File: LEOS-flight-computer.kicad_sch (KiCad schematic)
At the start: 7 parts, among them J3 GPIO

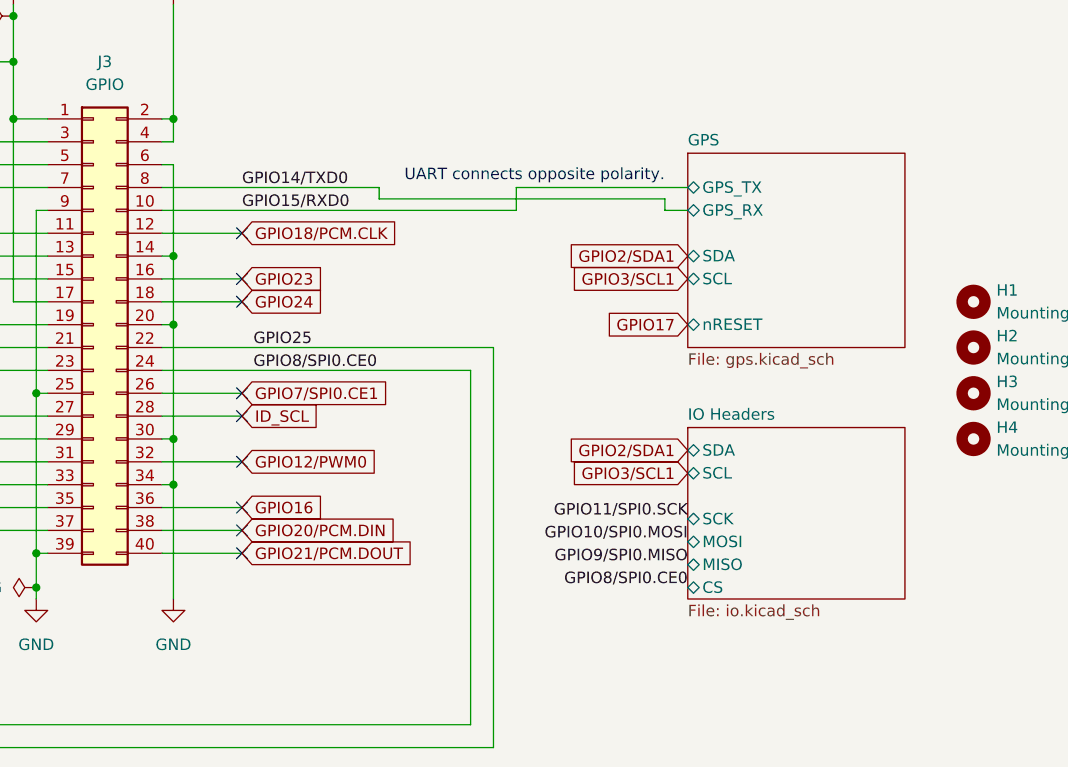
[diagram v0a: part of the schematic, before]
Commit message: v2.2 with added indicator LEDs and a user button
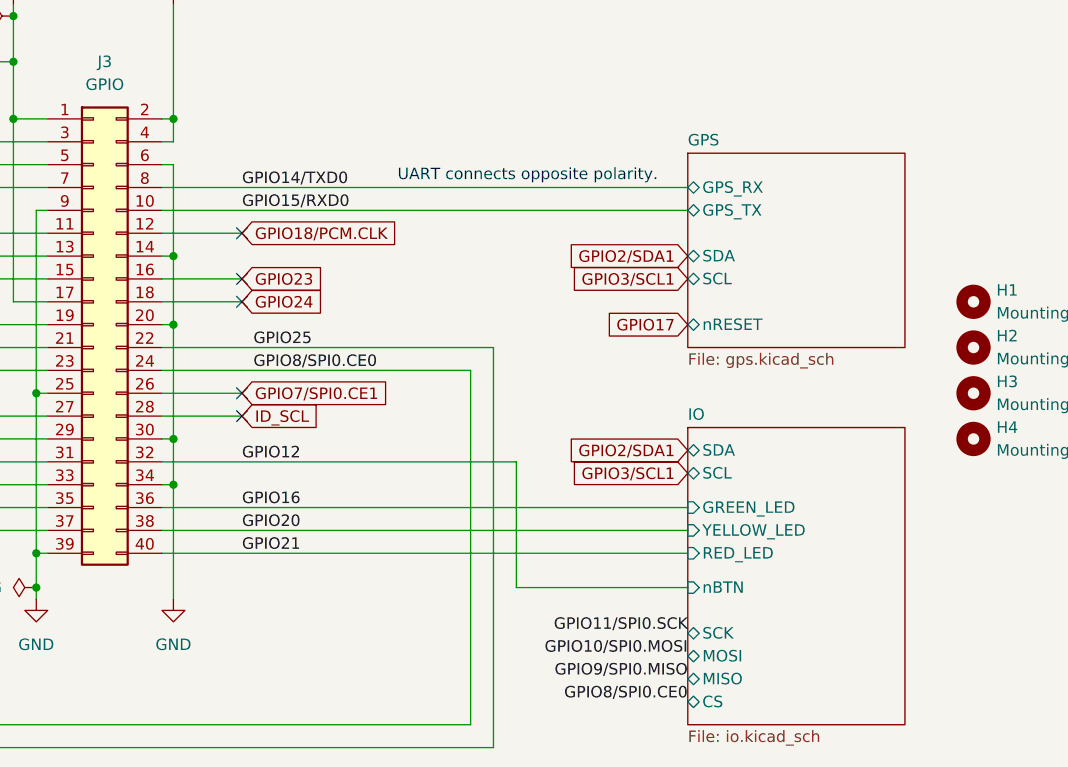
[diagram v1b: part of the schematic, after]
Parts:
- R2, R3: footprint Resistor_SMD:R_0603_1608Metric -> Resistor_SMD:R_0805_2012Metric; Digikey MCT0603-4.70K-CFCT-ND -> 541-4.70KCCT-ND; LCSC C23162 -> (none); MPN MCT06030C4701FP500 -> CRCW08054K70FKEA; Manufacturer Vishay -> Vishay Dale
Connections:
- net GPIO12/PWM0 renamed GPIO12
- net GPIO20/PCM.DIN renamed GPIO20
- net GPIO21/PCM.DOUT renamed GPIO21
- no-connect marks 18 -> 14
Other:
- sheet IO Headers renamed IO
- sheet IO ports: added GREEN_LED, RED_LED, YELLOW_LED, nBTN; removed none
